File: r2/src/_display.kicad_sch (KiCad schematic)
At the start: 10 parts, among them J4 AFC07-S40ECA-00, Q6 AP2302B

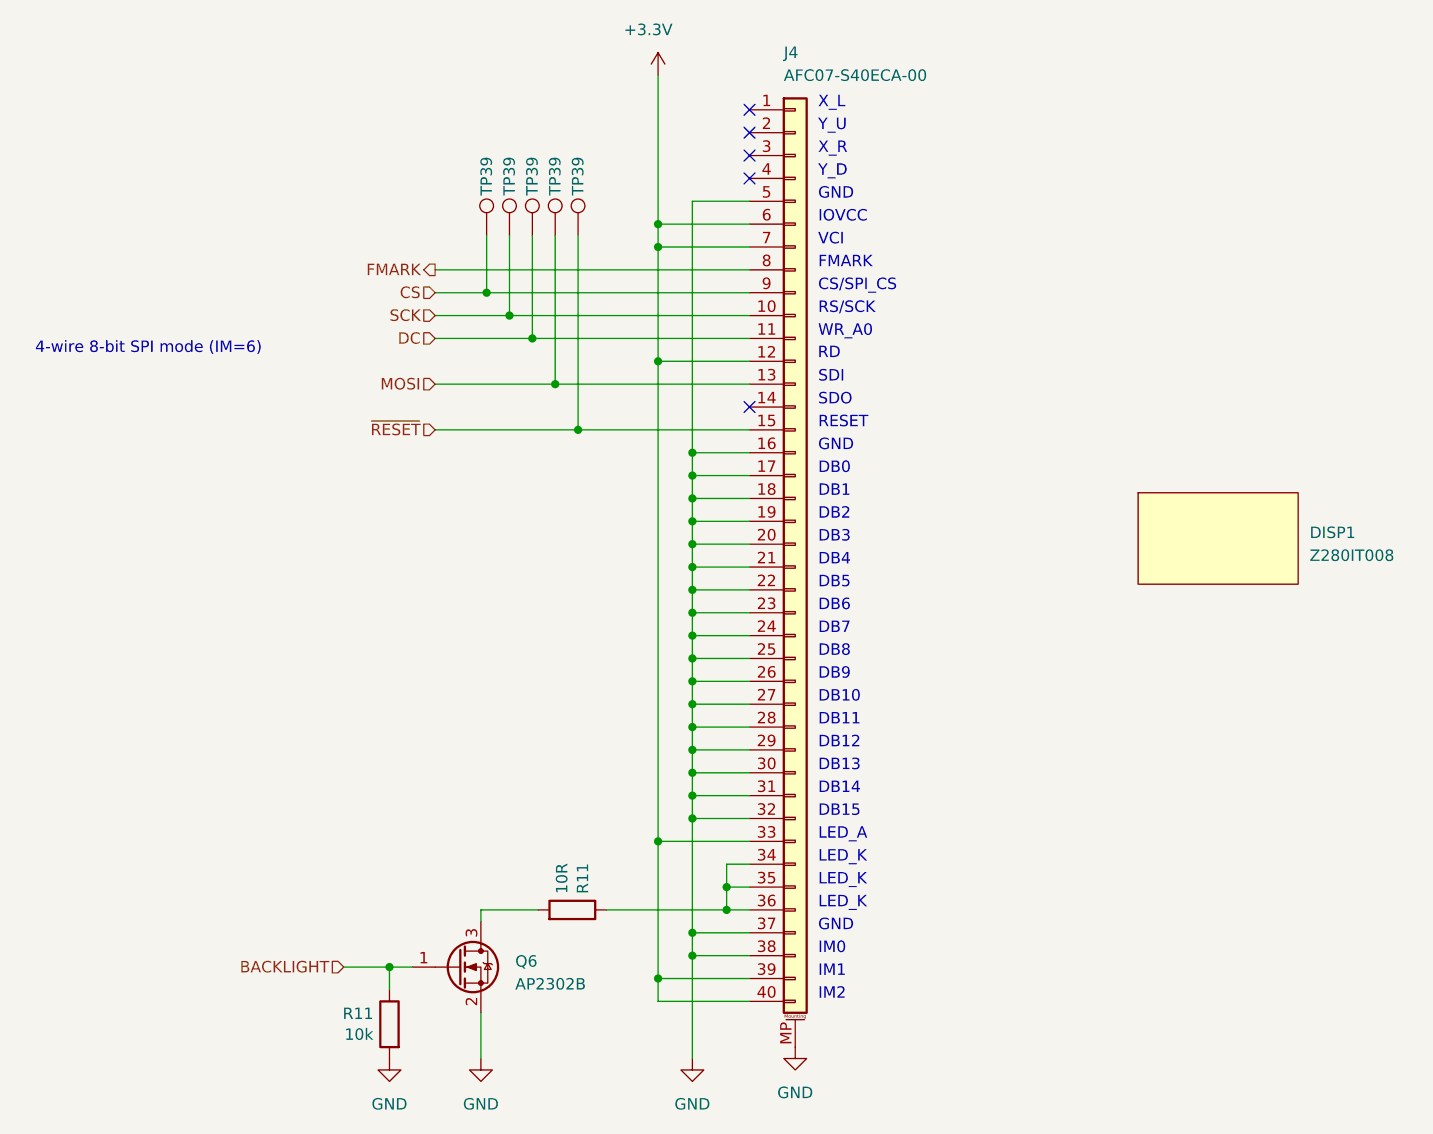
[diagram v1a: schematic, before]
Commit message: Fix off-grid ERC errors so whole schematic is on 1.27mm grid
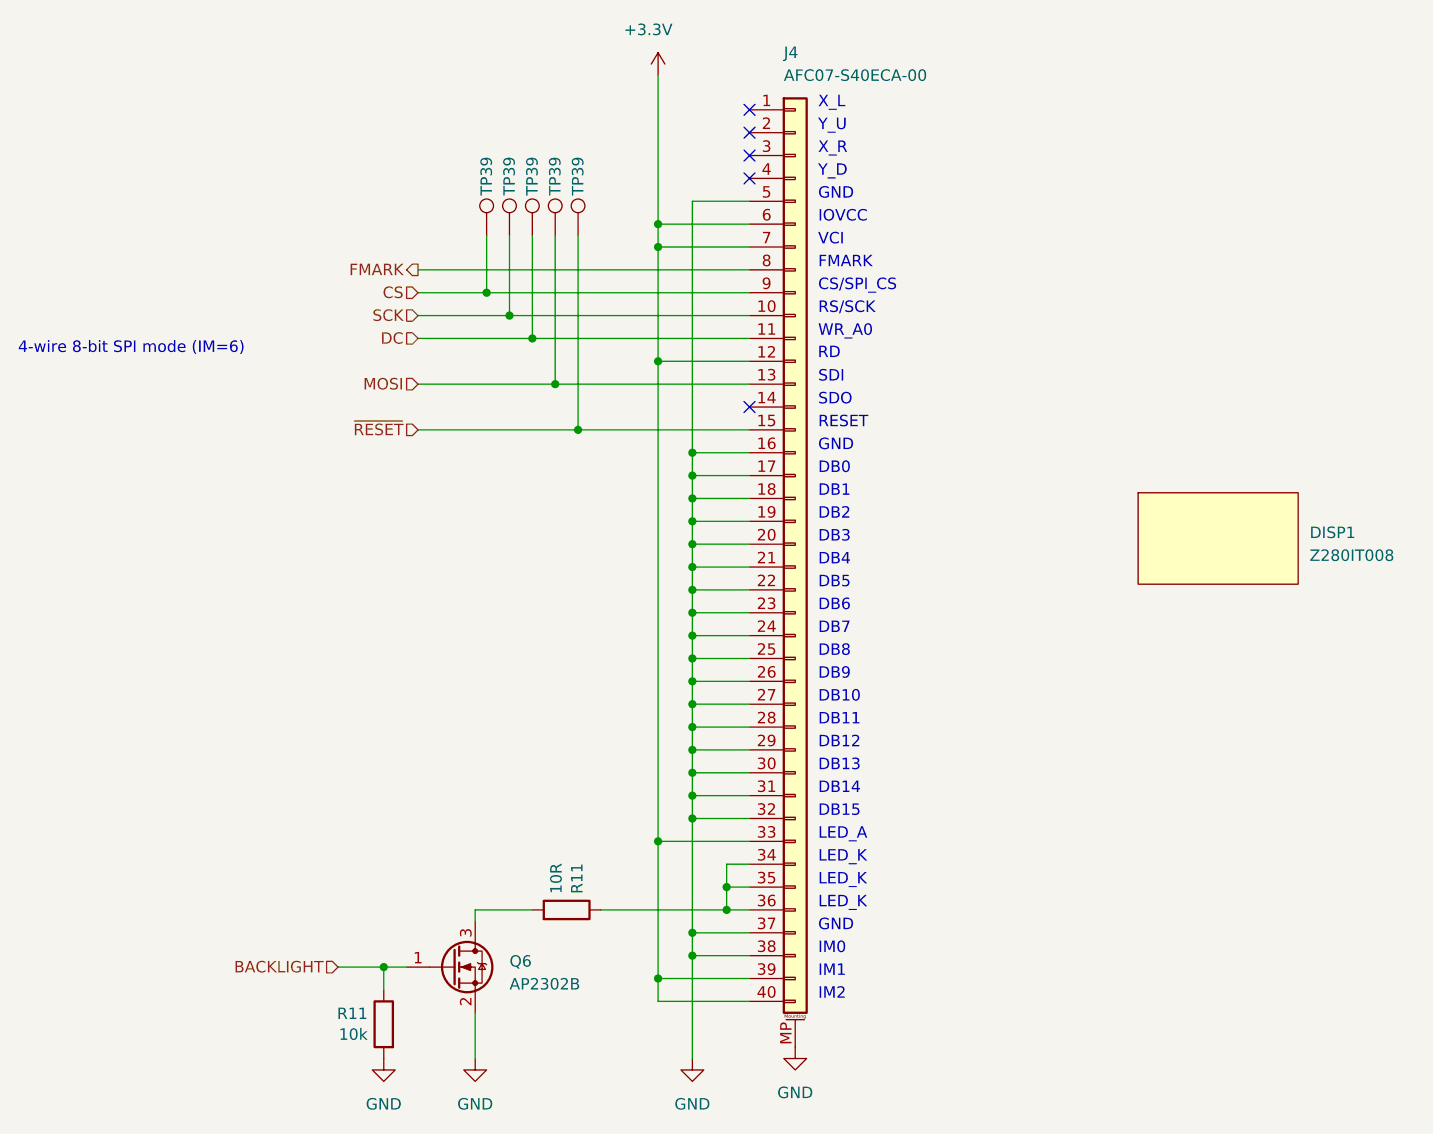
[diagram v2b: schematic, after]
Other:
- moved on the sheet: Q6, R11

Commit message: Set title block contents
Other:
- company: (none) -> Monad Gottfried Ltd. 2023
- title: (none) -> Troopers 23 Badge
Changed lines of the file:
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@@
 (kicad_sch (version 20230409) (generator eeschema)
   (paper "A4")
+  (title_block
+    (title "Troopers 23 Badge")
+    (rev "r2")
+    (company "Monad Gottfried Ltd. 2023")
+    (comment 1 "for ERNW Enno Rey Netzwerke GmbH")
+  )
   (junction (at 134.62 86.36) (diameter 0) (color 0 0 0 0)
   )
